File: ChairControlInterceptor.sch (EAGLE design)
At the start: 14 parts, among them J1 Digital_0_7, J2 Analog, J3 Digital_8_13, SW1 TL46WO, X1 INPUT, X2 OUTPUT

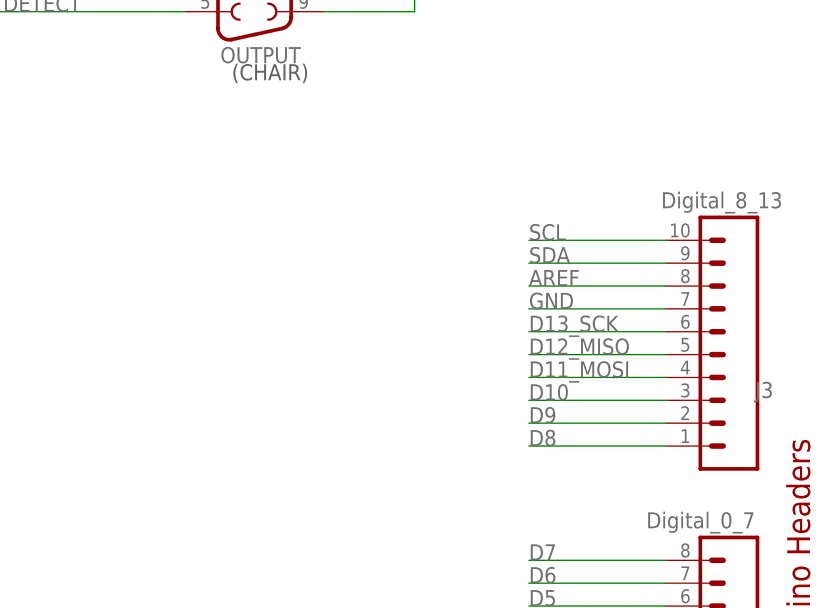
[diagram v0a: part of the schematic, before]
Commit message: Added Mini DIN-4 connector for Flysky trainer cable connection
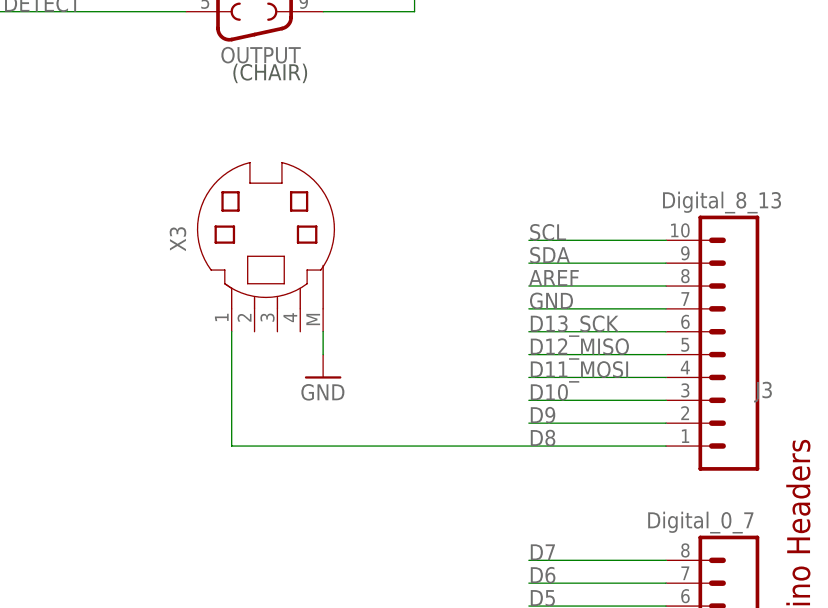
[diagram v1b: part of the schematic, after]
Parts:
- added X3: (no value), freetronics-jon:MD04S
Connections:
- net D8: now also X3.1
- net GND: now also X3.5
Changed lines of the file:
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@@
 <?xml version="1.0" encoding="utf-8"?>
 <!DOCTYPE eagle SYSTEM "eagle.dtd">
-<eagle version="8.5.1">
+<eagle version="8.6.0">
 <drawing>
 <settings>
@@
 <grid distance="0.1" unitdist="inch" unit="inch" style="lines" multiple="1" display="no" altdistance="0.01" altunitdist="inch" altunit="inch"/>
 <layers>
-<layer number="1" name="Top" color="4" fill="1" visible="no" active="no"/>
-<layer number="2" name="Route2" color="1" fill="3" visible="no" active="no"/>
-<layer number="15" name="Route15" color="4" fill="6" visible="no" active="no"/>
-<layer number="16" name="Bottom" color="1" fill="1" visible="no" active="no"/>
-<layer number="17" name="Pads" color="2" fill="1" visible="no" active="no"/>
-<layer number="18" name="Vias" color="2" fill="1" visible="no" active="no"/>
-<layer number="19" name="Unrouted" color="6" fill="1" visible="no" active="no"/>
-<layer number="20" name="Dimension" color="15" fill="1" visible="no" active="no"/>
-<layer number="21" name="tPlace" color="16" fill="1" visible="no" active="no"/>
-<layer number="22" name="bPlace" color="14" fill="1" visible="no" active="no"/>
-<layer number="23" name="tOrigins" color="15" fill="1" visible="no" active="no"/>
-<layer number="24" name="bOrigins" color="15" fill="1" visible="no" active="no"/>
-<layer number="25" name="tNames" color="7" fill="1" visible="no" active="no"/>
-<layer number="26" name="bNames" color="7" fill="1" visible="no" active="no"/>
-<layer number="27" name="tValues" color="7" fill="1" visible="no" active="no"/>
-<layer number="28" name="bValues" color="7" fill="1" visible="no" active="no"/>
+<layer number="1" name="Top" color="4" fill="1" visible="yes" active="no"/>
+<layer number="2" name="Route2" color="1" fill="3" visible="yes" active="no"/>
+<layer number="15" name="Route15" color="4" fill="6" visible="yes" active="no"/>
+<layer number="16" name="Bottom" color="1" fill="1" visible="yes" active="no"/>
+<layer number="17" name="Pads" color="2" fill="1" visible="yes" active="no"/>
+<layer number="18" name="Vias" color="2" fill="1" visible="yes" active="no"/>
+<layer number="19" name="Unrouted" color="12" fill="1" visible="yes" active="no"/>
+<layer number="20" name="Dimension" color="15" fill="1" visible="yes" active="no"/>
+<layer number="21" name="tPlace" color="15" fill="1" visible="yes" active="no"/>
+<layer number="22" name="bPlace" color="14" fill="1" visible="yes" active="no"/>
+<layer number="23" name="tOrigins" color="15" fill="1" visible="yes" active="no"/>
+<layer number="24" name="bOrigins" color="15" fill="1" visible="yes" active="no"/>
+<layer number="25" name="tNames" color="7" fill="1" visible="yes" active="no"/>
+<layer number="26" name="bNames" color="7" fill="1" visible="yes" active="no"/>
+<layer number="27" name="tValues" color="7" fill="1" visible="yes" active="no"/>
+<layer number="28" name="bValues" color="7" fill="1" visible="yes" active="no"/>
 <layer number="29" name="tStop" color="7" fill="3" visible="no" active="no"/>
 <layer number="30" name="bStop" color="7" fill="6" visible="no" active="no"/>
@@
 <layer number="35" name="tGlue" color="7" fill="4" visible="no" active="no"/>
 <layer number="36" name="bGlue" color="7" fill="5" visible="no" active="no"/>
-<layer number="37" name="tTest" color="7" fill="1" visible="no" active="no"/>
-<layer number="38" name="bTest" color="7" fill="1" visible="no" active="no"/>
+<layer number="37" name="tTest" color="7" fill="1" visible="yes" active="no"/>
+<layer number="38" name="bTest" color="7" fill="1" visible="yes" active="no"/>
 <layer number="39" name="tKeepout" color="4" fill="11" visible="no" active="no"/>
 <layer number="40" name="bKeepout" color="1" fill="11" visible="no" active="no"/>
@@
 <layer number="44" name="Drills" color="7" fill="1" visible="no" active="no"/>
 <layer number="45" name="Holes" color="7" fill="1" visible="no" active="no"/>
-<layer number="46" name="Milling" color="3" fill="1" visible="no" active="no"/>
-<layer number="47" name="Measures" color="7" fill="1" visible="no" active="no"/>
-<layer number="48" name="Document" color="7" fill="1" visible="no" active="no"/>
-<layer number="49" name="Reference" color="7" fill="1" visible="no" active="no"/>
-<layer number="50" name="dxf" color="7" fill="1" visible="no" active="no"/>
-<layer number="51" name="tDocu" color="6" fill="1" visible="no" active="no"/>
-<layer number="52" name="bDocu" color="7" fill="1" visible="no" active="no"/>
-<layer number="53" name="tGND_GNDA" color="7" fill="9" visible="no" active="no"/>
-<layer number="54" name="bGND_GNDA" color="1" fill="9" visible="no" active="no"/>
-<layer number="56" name="wert" color="7" fill="1" visible="no" active="no"/>
-<layer number="57" name="tCAD" color="7" fill="1" visible="no" active="no"/>
-<layer number="59" name="tCarbon" color="7" fill="1" visible="no" active="no"/>
-<layer number="60" name="bCarbon" color="7" fill="1" visible="no" active="no"/>
+<layer number="46" name="Milling" color="3" fill="1" visible="yes" active="no"/>
+<layer number="47" name="Measures" color="7" fill="1" visible="yes" active="no"/>
+<layer number="48" name="Document" color="7" fill="1" visible="yes" active="no"/>
+<layer number="49" name="Reference" color="7" fill="1" visible="yes" active="no"/>
+<layer number="50" name="dxf" color="7" fill="1" visible="yes" active="no"/>
+<layer number="51" name="tDocu" color="6" fill="1" visible="yes" active="no"/>
+<layer number="52" name="bDocu" color="7" fill="1" visible="yes" active="no"/>
+<layer number="53" name="tGND_GNDA" color="7" fill="9" visible="yes" active="no"/>
+<layer number="54" name="bGND_GNDA" color="1" fill="9" visible="yes" active="no"/>
+<layer number="56" name="wert" color="7" fill="1" visible="yes" active="no"/>
+<layer number="57" name="tCAD" color="7" fill="1" visible="yes" active="no"/>
+<layer number="59" name="tCarbon" color="7" fill="1" visible="yes" active="no"/>
+<layer number="60" name="bCarbon" color="7" fill="1" visible="yes" active="no"/>
 <layer number="88" name="SimResults" color="9" fill="1" visible="yes" active="yes"/>
 <layer number="89" name="SimProbes" color="9" fill="1" visible="yes" active="yes"/>
@@
 <part name="GND5" library="freetronics" deviceset="GND" device=""/>
 <part name="SW1" library="switch" library_urn="urn:adsk.eagle:library:380" deviceset="TL46WO" device="" package3d_urn="urn:adsk.eagle:package:27749/1"/>
+<part name="X3" library="freetronics-jon" deviceset="MD04S" device=""/>
+<part name="GND6" library="freetronics" deviceset="GND" device=""/>
 </parts>
 <sheets>
@@
 <instance part="GND5" gate="1" x="137.16" y="71.12"/>
 <instance part="SW1" gate="BEF1" x="119.38" y="152.4" rot="R270"/>
+<instance part="X3" gate="G$1" x="182.88" y="101.6" rot="R90"/>
+<instance part="GND6" gate="1" x="187.96" y="86.36"/>
 </instances>
 <busses>
@@
 <wire x1="137.16" y1="76.2" x2="137.16" y2="73.66" width="0.1524" layer="91"/>
 </segment>
+<segment>
+<pinref part="X3" gate="G$1" pin="5"/>
+<pinref part="GND6" gate="1" pin="GND"/>
+<wire x1="187.96" y1="91.44" x2="187.96" y2="88.9" width="0.1524" layer="91"/>
+</segment>
 </net>
 <net name="RESET" class="0">
@@
 <net name="D8" class="0">
 <segment>
-<wire x1="210.82" y1="78.74" x2="226.06" y2="78.74" width="0.1524" layer="91"/>
 <label x="210.82" y="78.74" size="1.778" layer="95"/>
 <pinref part="J3" gate="G$1" pin="1"/>
-</segment>
-</net>
+<pinref part="X3" gate="G$1" pin="1"/>
+<wire x1="177.8" y1="91.44" x2="177.8" y2="78.74" width="0.1524" layer="91"/>
+<wire x1="177.8" y1="78.74" x2="226.06" y2="78.74" width="0.1524" layer="91"/>
+</segment>
+</net>

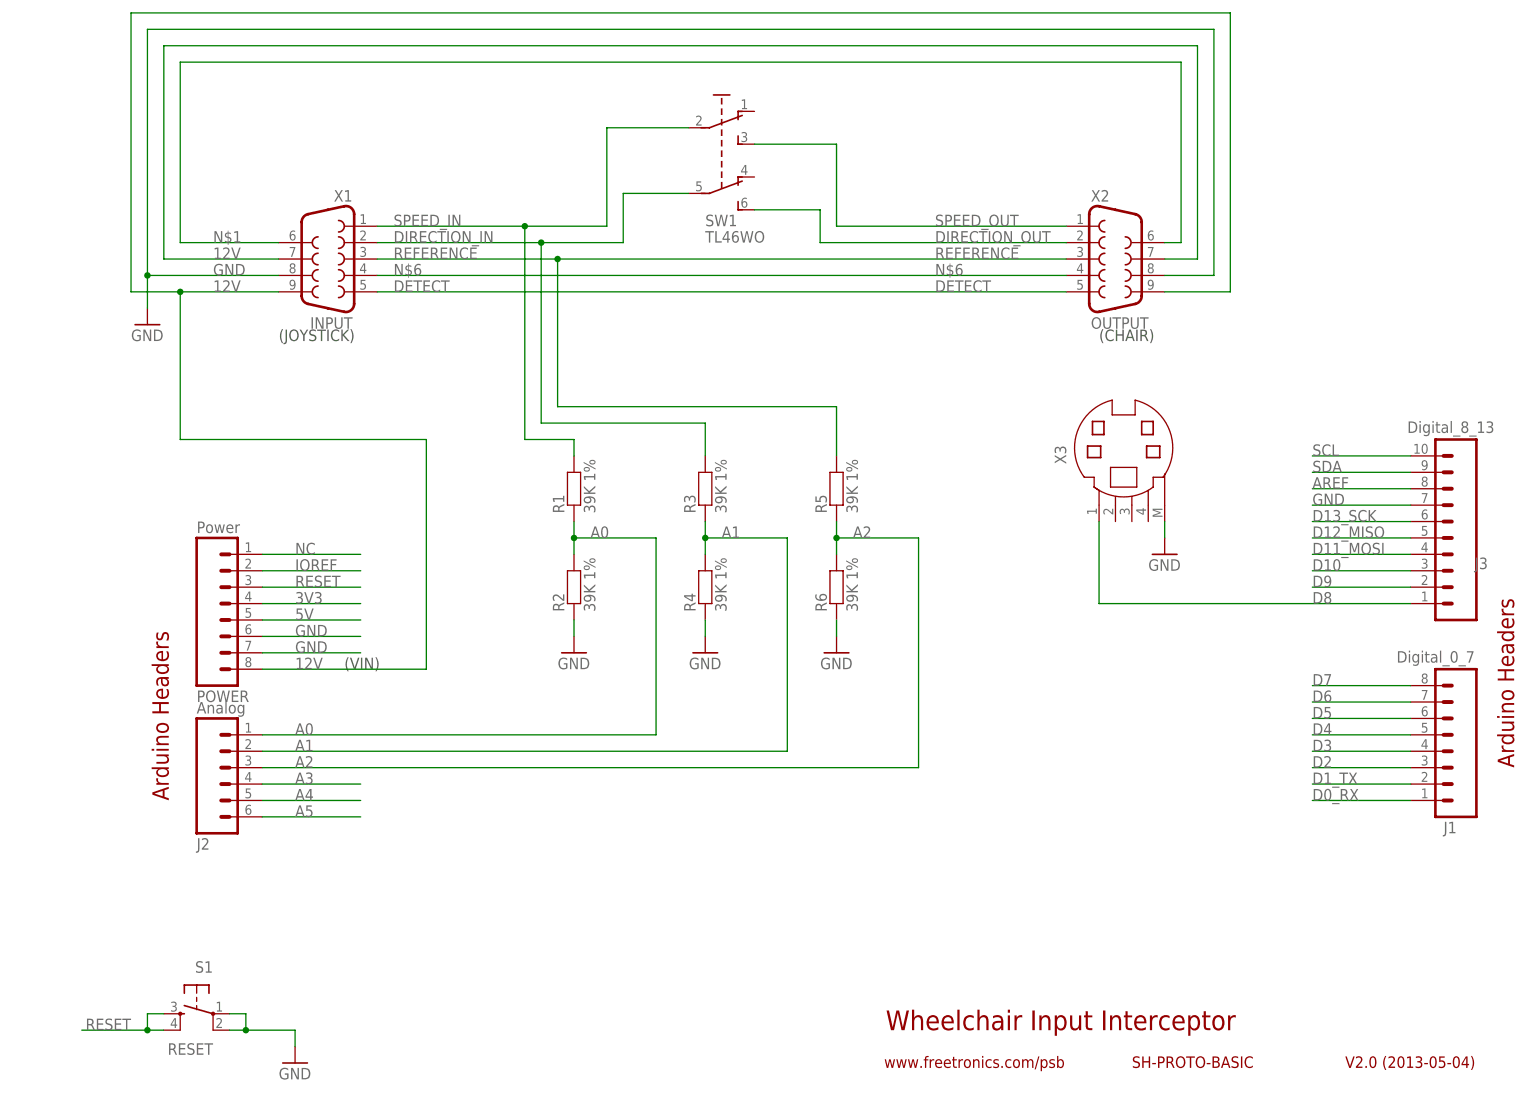
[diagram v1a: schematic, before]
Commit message: Added second joystick input and changed outline to suit HB5922 case
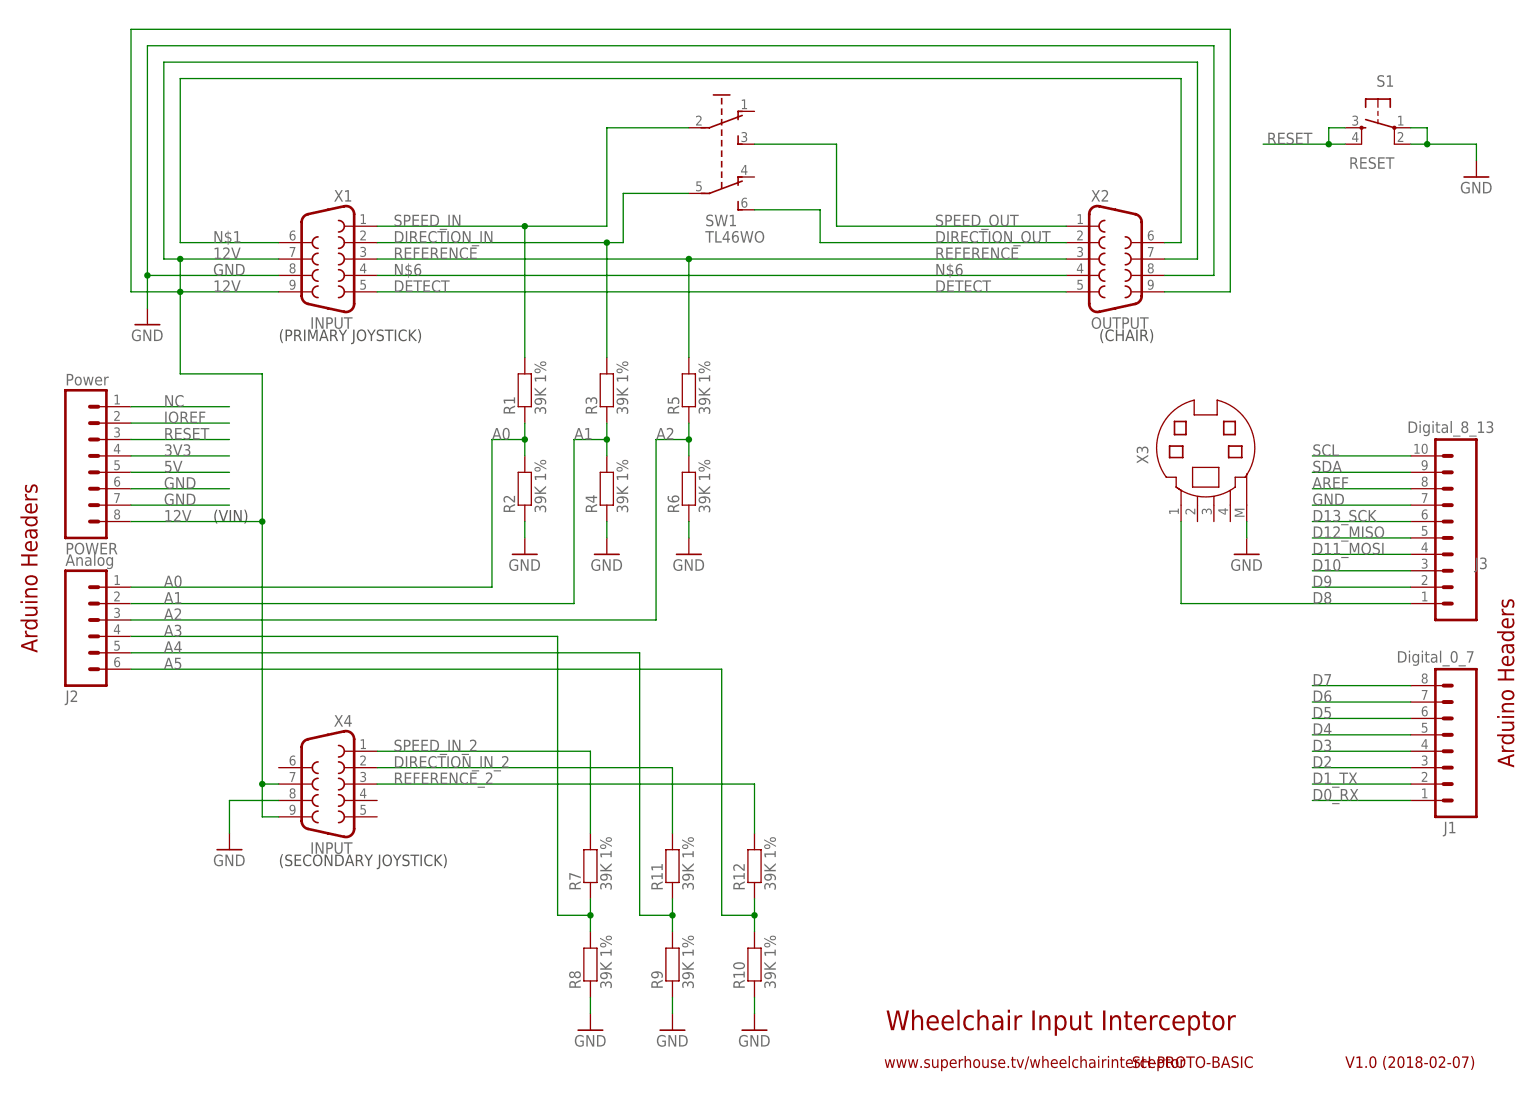
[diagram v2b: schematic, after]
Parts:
- added R10, R11, R12, R7, R8, R9: 39K 1%, freetronics-jon:RESISTOR0603
- added X4: INPUT, SparkFun-Connectors:DB9MALE
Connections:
- new net DIRECTION_IN_2: R11.2, X4.2
- new net REFERENCE_2: R12.2, X4.3
- new net SPEED_IN_2: R7.2, X4.1
- net 12V: now also X4.7, X4.9
- net A3: now also R7.1, R8.2
- net A4: now also R11.1, R9.2
- net A5: now also R10.2, R12.1
- net GND: now also R10.1, R8.1, R9.1, X4.8
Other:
- note added: "(PRIMARY JOYSTICK)"
- note added: "(SECONDARY JOYSTICK)"
- note added: "V1.0 (2018-02-07)"
- note added: "www.superhouse.tv/wheelchairinterceptor"
- note removed: "(JOYSTICK)"
- note removed: "V2.0 (2013-05-04)"
- note removed: "www.freetronics.com/psb"
- moved on the sheet: J2, POWER, R1, R2, R3, R4, R5, R6, S1, X3
